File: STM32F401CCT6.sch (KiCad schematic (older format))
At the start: 43 parts, among them J1 USB_OTG, J2 Conn_02x03_Odd_Even, J3 Conn_01x20_des, J4 Conn_01x05_desc, J5 Conn_01x20, SW1 SW_Push, U1 MIC5219-3.3, U2 STM32F401CCT6, U3 USBLC6-2SC6, Y1 32.786K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

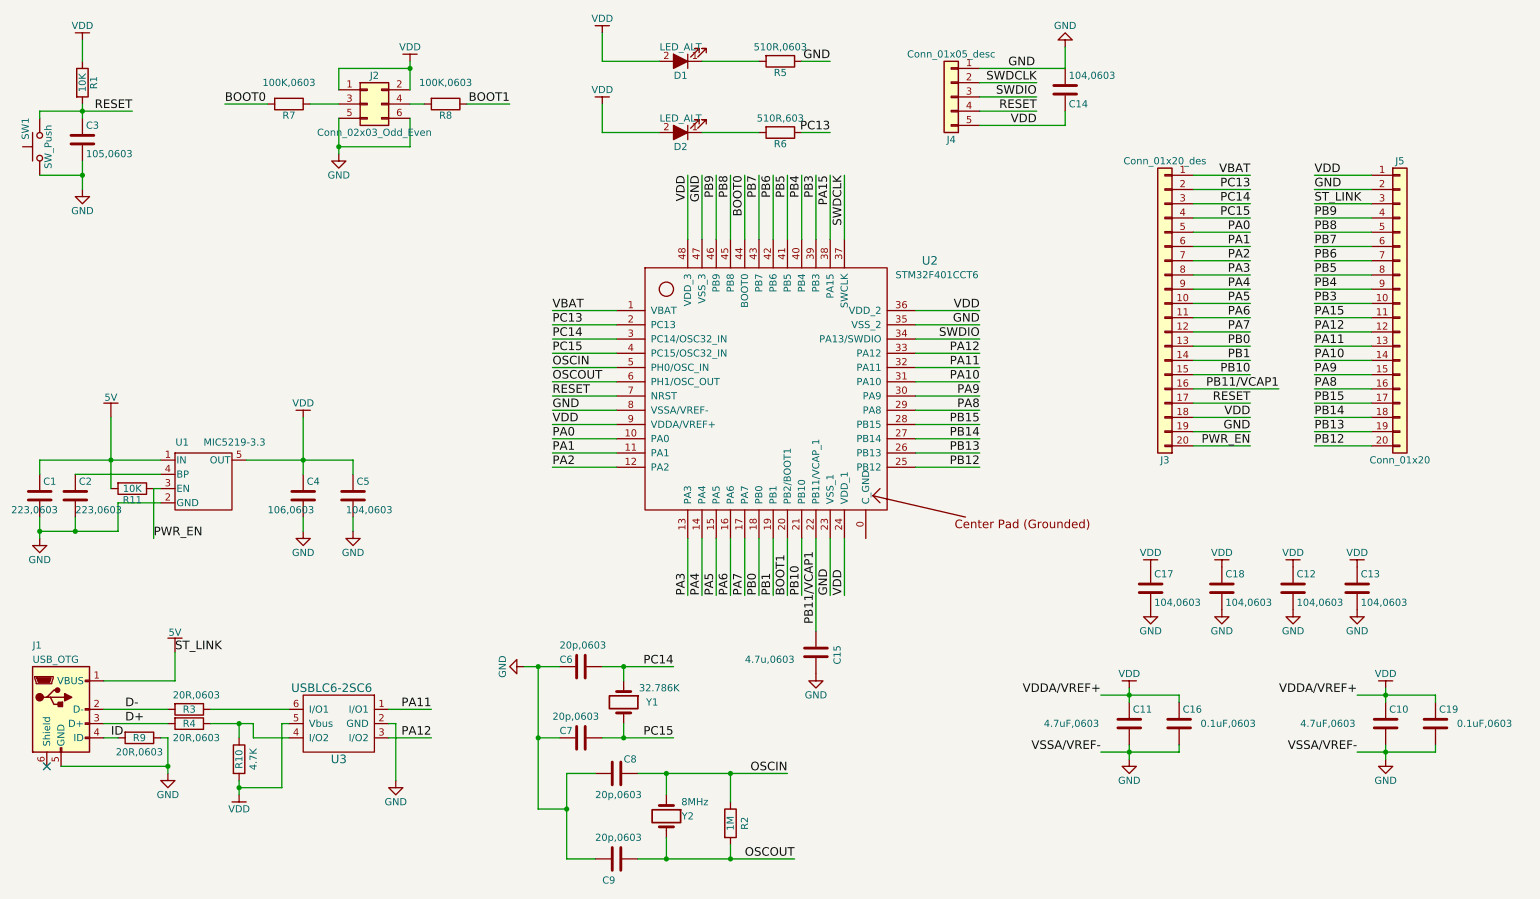
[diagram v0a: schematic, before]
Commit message: Change the route nicely
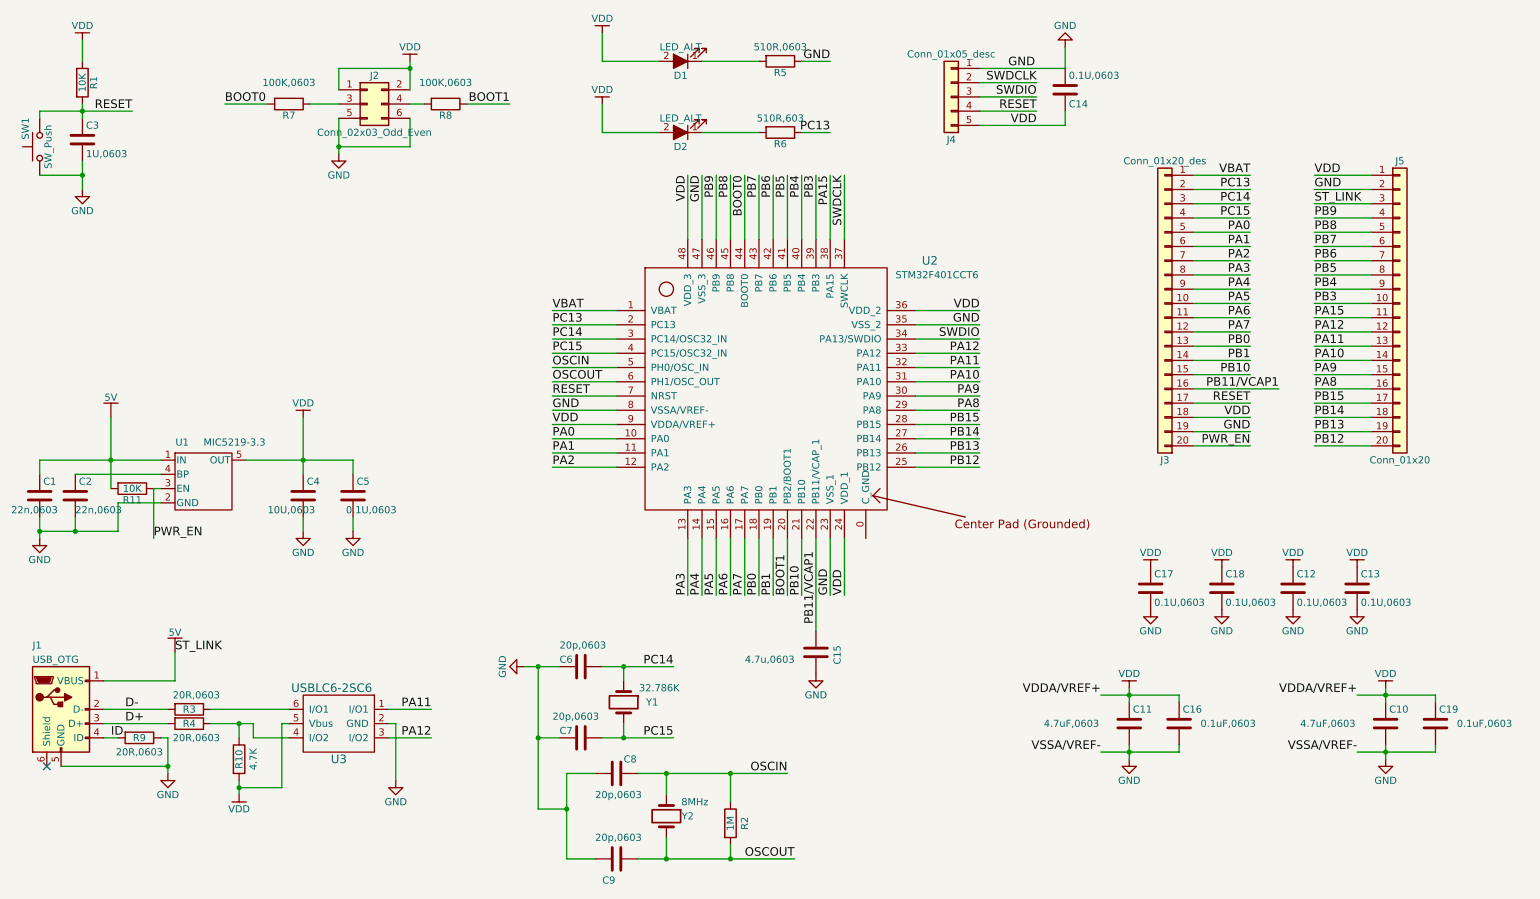
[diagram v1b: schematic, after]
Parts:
- C1, C2: value 223,0603 -> 22n,0603
- C12, C13, C14, C17, C18, C5: value 104,0603 -> 0.1U,0603
- C3: value 105,0603 -> 1U,0603
- C4: value 106,0603 -> 10U,0603
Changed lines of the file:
@@
 P 1050 1600
 F 0 "C3" H 1075 1700 50  0000 L CNN
-F 1 "105,0603" H 1075 1500 50  0000 L CNN
+F 1 "1U,0603" H 1075 1500 50  0000 L CNN
 F 2 "Capacitors_SMD:C_0603" H 1088 1450 50  0001 C CNN
 F 3 "" H 1050 1600 50  0001 C CNN
@@
 P 7950 1250
 F 0 "C14" H 7975 1350 50  0000 L CNN
-F 1 "104,0603" H 7975 1150 50  0000 L CNN
+F 1 "0.1U,0603" H 7975 1150 50  0000 L CNN
 F 2 "Capacitors_SMD:C_0603" H 7988 1100 50  0001 C CNN
 F 3 "" H 7950 1250 50  0001 C CNN
@@
 P 9550 4750
 F 0 "C12" H 9575 4850 50  0000 L CNN
-F 1 "104,0603" H 9575 4650 50  0000 L CNN
+F 1 "0.1U,0603" H 9575 4650 50  0000 L CNN
 F 2 "Capacitors_SMD:C_0603" H 9588 4600 50  0001 C CNN
 F 3 "" H 9550 4750 50  0001 C CNN
@@
 P 10000 4750
 F 0 "C13" H 10025 4850 50  0000 L CNN
-F 1 "104,0603" H 10025 4650 50  0000 L CNN
+F 1 "0.1U,0603" H 10025 4650 50  0000 L CNN
 F 2 "Capacitors_SMD:C_0603" H 10038 4600 50  0001 C CNN
 F 3 "" H 10000 4750 50  0001 C CNN
@@
 P 750 4100
 F 0 "C1" H 775 4200 50  0000 L CNN
-F 1 "223,0603" H 550 4000 50  0000 L CNN
+F 1 "22n,0603" H 550 4000 50  0000 L CNN
 F 2 "Capacitors_SMD:C_0603" H 788 3950 50  0001 C CNN
 F 3 "" H 750 4100 50  0001 C CNN
@@
 P 1000 4100
 F 0 "C2" H 1025 4200 50  0000 L CNN
-F 1 "223,0603" H 1000 4000 50  0000 L CNN
+F 1 "22n,0603" H 1000 4000 50  0000 L CNN
 F 2 "Capacitors_SMD:C_0603" H 1038 3950 50  0001 C CNN
 F 3 "" H 1000 4100 50  0001 C CNN
@@
 P 2600 4100
 F 0 "C4" H 2625 4200 50  0000 L CNN
-F 1 "106,0603" H 2350 4000 50  0000 L CNN
+F 1 "10U,0603" H 2350 4000 50  0000 L CNN
 F 2 "Capacitors_SMD:C_0603" H 2638 3950 50  0001 C CNN
 F 3 "" H 2600 4100 50  0001 C CNN
@@
 P 2950 4100
 F 0 "C5" H 2975 4200 50  0000 L CNN
-F 1 "104,0603" H 2900 4000 50  0000 L CNN
+F 1 "0.1U,0603" H 2900 4000 50  0000 L CNN
 F 2 "Capacitors_SMD:C_0603" H 2988 3950 50  0001 C CNN
 F 3 "" H 2950 4100 50  0001 C CNN
@@
 P 9050 4750
 F 0 "C18" H 9075 4850 50  0000 L CNN
-F 1 "104,0603" H 9075 4650 50  0000 L CNN
+F 1 "0.1U,0603" H 9075 4650 50  0000 L CNN
 F 2 "Capacitors_SMD:C_0603" H 9088 4600 50  0001 C CNN
 F 3 "" H 9050 4750 50  0001 C CNN
@@
 P 8550 4750
 F 0 "C17" H 8575 4850 50  0000 L CNN
-F 1 "104,0603" H 8575 4650 50  0000 L CNN
+F 1 "0.1U,0603" H 8575 4650 50  0000 L CNN
 F 2 "Capacitors_SMD:C_0603" H 8588 4600 50  0001 C CNN
 F 3 "" H 8550 4750 50  0001 C CNN

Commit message: Renamed the pin3 track label from ST-Link to Vin
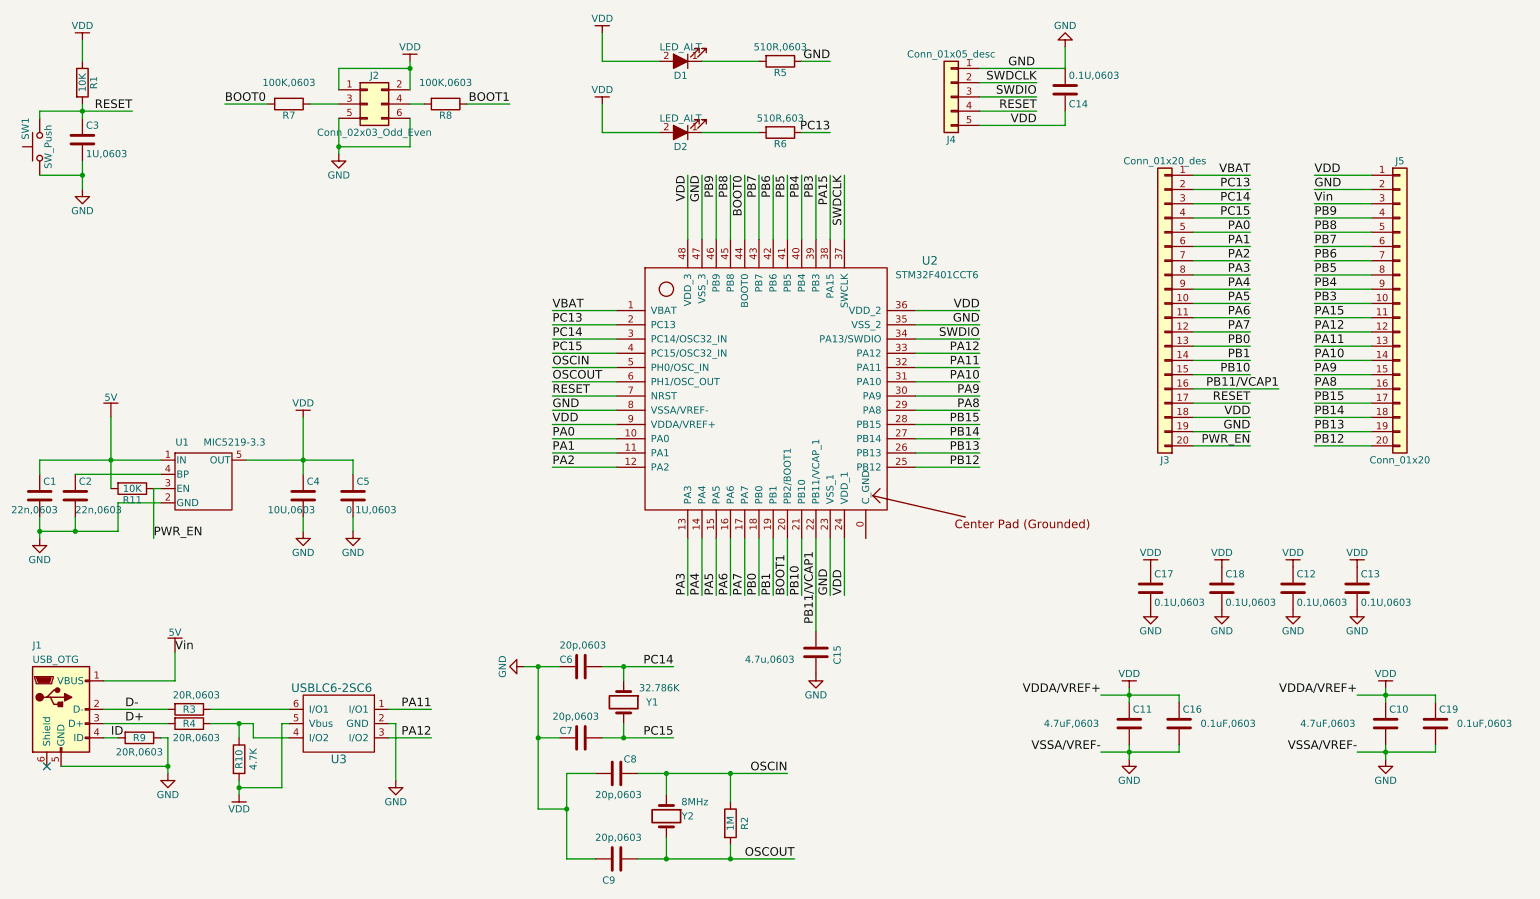
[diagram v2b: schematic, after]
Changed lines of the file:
@@
 GND
 Text Label 9700 2050 0    60   ~ 0
-ST_LINK
+Vin
 Text Label 9700 2150 0    60   ~ 0
 PB9
@@
 GND
 Text Label 1700 5200 0    60   ~ 0
-ST_LINK
+Vin
 $Comp
 L LED_ALT D1

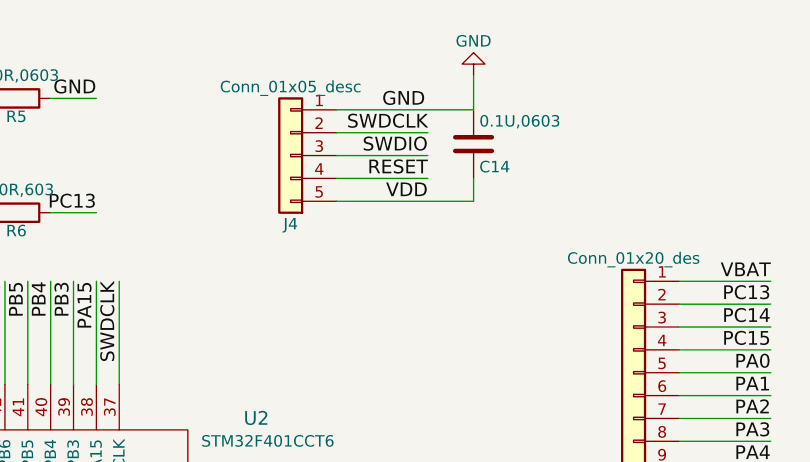
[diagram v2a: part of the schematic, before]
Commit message: Moved silk layer away from via and swap the position of VDD with nRST pin of the SWDIO
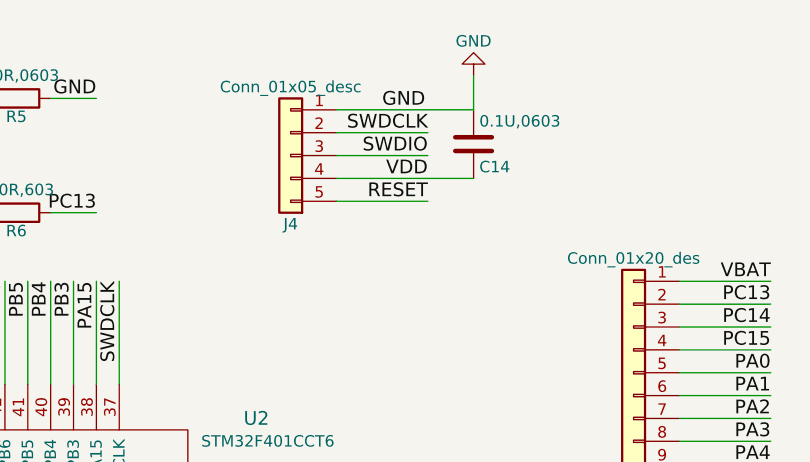
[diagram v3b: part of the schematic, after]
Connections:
- net RESET: now also J4.5 (Pin_5); no longer J4.4 (Pin_4)
- net VDD: now also J4.4 (Pin_4); no longer J4.5 (Pin_5)

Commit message: Replace the Micro-USB footprint with the one newly created, added a shield for MCU (grounded pin), moved some component inwards to prevent touching the pinheader plastic.
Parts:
- D1: value LED_ALT -> RED_LED
- D2: value LED_ALT -> BLUE_LED
- U2: footprint QFPN48:QFN_QFP48 -> (none)
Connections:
- net GND: now also J1.6 (Shield), U2.0 (C_GND)
- no-connect marks 1 -> 0
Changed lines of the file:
@@
 $EndComp
 $Comp
-L GND #PWR01
+L GND #PWR10
 U 1 1 59D25E0A
 P 2850 1700
-F 0 "#PWR01" H 2850 1450 50  0001 C CNN
+F 0 "#PWR10" H 2850 1450 50  0001 C CNN
 F 1 "GND" H 2850 1550 50  0000 C CNN
 F 2 "" H 2850 1700 50  0001 C CNN
@@
 RESET
 $Comp
-L GND #PWR02
+L GND #PWR3
 U 1 1 59D2716C
 P 1050 1950
-F 0 "#PWR02" H 1050 1700 50  0001 C CNN
+F 0 "#PWR3" H 1050 1700 50  0001 C CNN
 F 1 "GND" H 1050 1800 50  0000 C CNN
 F 2 "" H 1050 1950 50  0001 C CNN
@@
 $EndComp
 $Comp
-L 5V #PWR03
+L 5V #PWR6
 U 1 1 59D2797D
 P 1700 5200
-F 0 "#PWR03" H 1700 5050 50  0001 C CNN
+F 0 "#PWR6" H 1700 5050 50  0001 C CNN
 F 1 "5V" H 1700 5340 50  0000 C CNN
 F 2 "" H 1700 5200 50  0001 C CNN
@@
 	1    0    0    -1
 $EndComp
-NoConn ~ 800  6000
 $Comp
 L C C6
@@
 $EndComp
 $Comp
-L GND #PWR04
+L GND #PWR14
 U 1 1 59D289B6
 P 4150 5300
-F 0 "#PWR04" H 4150 5050 50  0001 C CNN
+F 0 "#PWR14" H 4150 5050 50  0001 C CNN
 F 1 "GND" H 4150 5150 50  0000 C CNN
 F 2 "" H 4150 5300 50  0001 C CNN
@@
 $EndComp
 $Comp
-L GND #PWR05
+L GND #PWR31
 U 1 1 59D28EE2
 P 10200 5950
-F 0 "#PWR05" H 10200 5700 50  0001 C CNN
+F 0 "#PWR31" H 10200 5700 50  0001 C CNN
 F 1 "GND" H 10200 5800 50  0000 C CNN
 F 2 "" H 10200 5950 50  0001 C CNN
@@
 $EndComp
 $Comp
-L GND #PWR06
+L GND #PWR27
 U 1 1 59D2CC17
 P 9550 4900
-F 0 "#PWR06" H 9550 4650 50  0001 C CNN
+F 0 "#PWR27" H 9550 4650 50  0001 C CNN
 F 1 "GND" H 9550 4750 50  0000 C CNN
 F 2 "" H 9550 4900 50  0001 C CNN
@@
 $EndComp
 $Comp
-L GND #PWR07
+L GND #PWR29
 U 1 1 59D2CC9A
 P 10000 4900
-F 0 "#PWR07" H 10000 4650 50  0001 C CNN
+F 0 "#PWR29" H 10000 4650 50  0001 C CNN
 F 1 "GND" H 10000 4750 50  0000 C CNN
 F 2 "" H 10000 4900 50  0001 C CNN
@@
 $EndComp
 $Comp
-L GND #PWR08
+L GND #PWR5
 U 1 1 59D2D880
 P 1650 6050
-F 0 "#PWR08" H 1650 5800 50  0001 C CNN
+F 0 "#PWR5" H 1650 5800 50  0001 C CNN
 F 1 "GND" H 1650 5900 50  0000 C CNN
 F 2 "" H 1650 6050 50  0001 C CNN
@@
 $EndComp
 $Comp
-L GND #PWR09
+L GND #PWR1
 U 1 1 59D37486
 P 750 4400
-F 0 "#PWR09" H 750 4150 50  0001 C CNN
+F 0 "#PWR1" H 750 4150 50  0001 C CNN
 F 1 "GND" H 750 4250 50  0000 C CNN
 F 2 "" H 750 4400 50  0001 C CNN
@@
 $EndComp
 $Comp
-L 5V #PWR010
+L 5V #PWR4
 U 1 1 59D374F7
 P 1250 3550
-F 0 "#PWR010" H 1250 3400 50  0001 C CNN
+F 0 "#PWR4" H 1250 3400 50  0001 C CNN
 F 1 "5V" H 1250 3690 50  0000 C CNN
 F 2 "" H 1250 3550 50  0001 C CNN
@@
 $EndComp
 $Comp
-L GND #PWR011
+L GND #PWR9
 U 1 1 59D37C81
 P 2600 4350
-F 0 "#PWR011" H 2600 4100 50  0001 C CNN
+F 0 "#PWR9" H 2600 4100 50  0001 C CNN
 F 1 "GND" H 2600 4200 50  0000 C CNN
 F 2 "" H 2600 4350 50  0001 C CNN
@@
 $EndComp
 $Comp
-L GND #PWR012
+L GND #PWR11
 U 1 1 59D37D1C
 P 2950 4350
-F 0 "#PWR012" H 2950 4100 50  0001 C CNN
+F 0 "#PWR11" H 2950 4100 50  0001 C CNN
 F 1 "GND" H 2950 4200 50  0000 C CNN
 F 2 "" H 2950 4350 50  0001 C CNN
@@
 $EndComp
 $Comp
-L GND #PWR013
+L GND #PWR19
 U 1 1 59D379C4
 P 7950 950
-F 0 "#PWR013" H 7950 700 50  0001 C CNN
+F 0 "#PWR19" H 7950 700 50  0001 C CNN
 F 1 "GND" H 7950 800 50  0000 C CNN
 F 2 "" H 7950 950 50  0001 C CNN
@@
 $EndComp
 $Comp
-L GND #PWR014
+L GND #PWR12
 U 1 1 59D3C918
 P 3250 6100
-F 0 "#PWR014" H 3250 5850 50  0001 C CNN
+F 0 "#PWR12" H 3250 5850 50  0001 C CNN
 F 1 "GND" H 3250 5950 50  0000 C CNN
 F 2 "" H 3250 6100 50  0001 C CNN
@@
 P 5250 1050
 F 0 "D1" H 5250 1150 50  0000 C CNN
-F 1 "LED_ALT" H 5250 950 50  0000 C CNN
+F 1 "RED_LED" H 5250 900 50  0000 C CNN
 F 2 "LEDs:LED_0805" H 5250 1050 50  0001 C CNN
 F 3 "" H 5250 1050 50  0001 C CNN
@@
 P 5250 1550
 F 0 "D2" H 5250 1650 50  0000 C CNN
-F 1 "LED_ALT" H 5250 1450 50  0000 C CNN
+F 1 "BLUE_LED" H 5250 1400 50  0000 C CNN
 F 2 "LEDs:LED_0805" H 5250 1550 50  0001 C CNN
 F 3 "" H 5250 1550 50  0001 C CNN
@@
 PB11/VCAP1
 $Comp
-L GND #PWR015
+L GND #PWR17
 U 1 1 59FD831D
 P 6200 5350
-F 0 "#PWR015" H 6200 5100 50  0001 C CNN
+F 0 "#PWR17" H 6200 5100 50  0001 C CNN
 F 1 "GND" H 6200 5200 50  0000 C CNN
 F 2 "" H 6200 5350 50  0001 C CNN
@@
 $EndComp
 $Comp
-L GND #PWR016
+L GND #PWR21
 U 1 1 5A0064D3
 P 8400 5950
-F 0 "#PWR016" H 8400 5700 50  0001 C CNN
+F 0 "#PWR21" H 8400 5700 50  0001 C CNN
 F 1 "GND" H 8400 5800 50  0000 C CNN
 F 2 "" H 8400 5950 50  0001 C CNN
@@
 $EndComp
 $Comp
-L GND #PWR017
+L GND #PWR25
 U 1 1 5A006C4E
 P 9050 4900
-F 0 "#PWR017" H 9050 4650 50  0001 C CNN
+F 0 "#PWR25" H 9050 4650 50  0001 C CNN
 F 1 "GND" H 9050 4750 50  0000 C CNN
 F 2 "" H 9050 4900 50  0001 C CNN
@@
 $EndComp
 $Comp
-L GND #PWR018
+L GND #PWR23
 U 1 1 5A006D37
 P 8550 4900
-F 0 "#PWR018" H 8550 4650 50  0001 C CNN
+F 0 "#PWR23" H 8550 4650 50  0001 C CNN
 F 1 "GND" H 8550 4750 50  0000 C CNN
 F 2 "" H 8550 4900 50  0001 C CNN
 F 3 "" H 8550 4900 50  0001 C CNN
 	1    8550 4900
-	1    0    0    -1
-$EndComp
-$Comp
-L STM32F401CCT6 U2
-U 1 1 5A00751A
-P 5450 3050
-F 0 "U2" H 7000 3650 60  0000 C CNN
-F 1 "STM32F401CCT6" H 7050 3550 50  0000 C CNN
-F 2 "QFPN48:QFN_QFP48" H 5450 3050 60  0001 C CNN
-F 3 "" H 5450 3050 60  0001 C CNN
-	1    5450 3050
 	1    0    0    -1
 $EndComp
@@
 PWR_EN
 $Comp
-L VDD-RESCUE-STM32F401CCT6 #PWR019
+L VDD-RESCUE-STM32F401CCT6 #PWR13
 U 1 1 5A056104
 P 3350 1050
-F 0 "#PWR019" H 3350 900 50  0001 C CNN
+F 0 "#PWR13" H 3350 900 50  0001 C CNN
 F 1 "VDD" H 3350 1150 50  0000 C CNN
 F 2 "" H 3350 1050 50  0001 C CNN
@@
 $EndComp
 $Comp
-L VDD-RESCUE-STM32F401CCT6 #PWR020
+L VDD-RESCUE-STM32F401CCT6 #PWR2
 U 1 1 5A0564A9
 P 1050 900
-F 0 "#PWR020" H 1050 750 50  0001 C CNN
+F 0 "#PWR2" H 1050 750 50  0001 C CNN
 F 1 "VDD" H 1050 1000 50  0000 C CNN
 F 2 "" H 1050 900 50  0001 C CNN
@@
 $EndComp
 $Comp
-L VDD-RESCUE-STM32F401CCT6 #PWR021
+L VDD-RESCUE-STM32F401CCT6 #PWR15
 U 1 1 5A05668E
 P 4700 850
-F 0 "#PWR021" H 4700 700 50  0001 C CNN
+F 0 "#PWR15" H 4700 700 50  0001 C CNN
 F 1 "VDD" H 4700 950 50  0000 C CNN
 F 2 "" H 4700 850 50  0001 C CNN
@@
 $EndComp
 $Comp
-L VDD-RESCUE-STM32F401CCT6 #PWR022
+L VDD-RESCUE-STM32F401CCT6 #PWR16
 U 1 1 5A056771
 P 4700 1350
-F 0 "#PWR022" H 4700 1200 50  0001 C CNN
+F 0 "#PWR16" H 4700 1200 50  0001 C CNN
 F 1 "VDD" H 4700 1450 50  0000 C CNN
 F 2 "" H 4700 1350 50  0001 C CNN
@@
 $EndComp
 $Comp
-L VDD-RESCUE-STM32F401CCT6 #PWR023
+L VDD-RESCUE-STM32F401CCT6 #PWR22
 U 1 1 5A056DEA
 P 8550 4600
-F 0 "#PWR023" H 8550 4450 50  0001 C CNN
+F 0 "#PWR22" H 8550 4450 50  0001 C CNN
 F 1 "VDD" H 8550 4700 50  0000 C CNN
 F 2 "" H 8550 4600 50  0001 C CNN
@@
 $EndComp
 $Comp
-L VDD-RESCUE-STM32F401CCT6 #PWR024
+L VDD-RESCUE-STM32F401CCT6 #PWR24
 U 1 1 5A0570FB
 P 9050 4600
-F 0 "#PWR024" H 9050 4450 50  0001 C CNN
+F 0 "#PWR24" H 9050 4450 50  0001 C CNN
 F 1 "VDD" H 9050 4700 50  0000 C CNN
 F 2 "" H 9050 4600 50  0001 C CNN
@@
 $EndComp
 $Comp
-L VDD-RESCUE-STM32F401CCT6 #PWR025
+L VDD-RESCUE-STM32F401CCT6 #PWR26
 U 1 1 5A057187
 P 9550 4600
-F 0 "#PWR025" H 9550 4450 50  0001 C CNN
+F 0 "#PWR26" H 9550 4450 50  0001 C CNN
 F 1 "VDD" H 9550 4700 50  0000 C CNN
 F 2 "" H 9550 4600 50  0001 C CNN
@@
 $EndComp
 $Comp
-L VDD-RESCUE-STM32F401CCT6 #PWR026
+L VDD-RESCUE-STM32F401CCT6 #PWR28
 U 1 1 5A057213
 P 10000 4600
-F 0 "#PWR026" H 10000 4450 50  0001 C CNN
+F 0 "#PWR28" H 10000 4450 50  0001 C CNN
 F 1 "VDD" H 10000 4700 50  0000 C CNN
 F 2 "" H 10000 4600 50  0001 C CNN
@@
 $EndComp
 $Comp
-L VDD-RESCUE-STM32F401CCT6 #PWR027
+L VDD-RESCUE-STM32F401CCT6 #PWR20
 U 1 1 5A0574FD
 P 8400 5450
-F 0 "#PWR027" H 8400 5300 50  0001 C CNN
+F 0 "#PWR20" H 8400 5300 50  0001 C CNN
 F 1 "VDD" H 8400 5550 50  0000 C CNN
 F 2 "" H 8400 5450 50  0001 C CNN
@@
 $EndComp
 $Comp
-L VDD-RESCUE-STM32F401CCT6 #PWR028
+L VDD-RESCUE-STM32F401CCT6 #PWR30
 U 1 1 5A057589
 P 10200 5450
-F 0 "#PWR028" H 10200 5300 50  0001 C CNN
+F 0 "#PWR30" H 10200 5300 50  0001 C CNN
 F 1 "VDD" H 10200 5550 50  0000 C CNN
 F 2 "" H 10200 5450 50  0001 C CNN
@@
 $EndComp
 $Comp
-L VDD-RESCUE-STM32F401CCT6 #PWR029
+L VDD-RESCUE-STM32F401CCT6 #PWR8
 U 1 1 5A0578C6
 P 2600 3550
-F 0 "#PWR029" H 2600 3400 50  0001 C CNN
+F 0 "#PWR8" H 2600 3400 50  0001 C CNN
 F 1 "VDD" H 2600 3650 50  0000 C CNN
 F 2 "" H 2600 3550 50  0001 C CNN
@@
 $EndComp
 $Comp
-L VDD-RESCUE-STM32F401CCT6 #PWR030
+L VDD-RESCUE-STM32F401CCT6 #PWR7
 U 1 1 5A057BAF
 P 2150 6200
-F 0 "#PWR030" H 2150 6050 50  0001 C CNN
+F 0 "#PWR7" H 2150 6050 50  0001 C CNN
 F 1 "VDD" H 2150 6300 50  0000 C CNN
 F 2 "" H 2150 6200 50  0001 C CNN
@@
 	-1   0    0    1
 $EndComp
+$Comp
+L STM32F401CCT6 U2
+U 1 1 5A1585BD
+P 5450 3050
+F 0 "U2" H 7000 3650 60  0000 C CNN
+F 1 "STM32F401CCT6" H 7050 3550 50  0000 C CNN
+F 2 "" H 5450 3050 60  0001 C CNN
+F 3 "" H 5450 3050 60  0001 C CNN
+	1    5450 3050
+	1    0    0    -1
+$EndComp
 Wire Wire Line
 	2450 6150 2150 6150
@@
 	2150 6100 2150 6200
 Wire Wire Line
-	900  6000 1650 6000
+	800  6000 1650 6000
 Wire Wire Line
 	1200 5600 1650 5600
@@
 Wire Wire Line
 	7350 1500 7750 1500
+Connection ~ 900  6000
+Wire Wire Line
+	6550 4400 6550 4800
+$Comp
+L GND #PWR18
+U 1 1 5A158D06
+P 6550 4800
+F 0 "#PWR18" H 6550 4550 50  0001 C CNN
+F 1 "GND" H 6550 4650 50  0000 C CNN
+F 2 "" H 6550 4800 50  0001 C CNN
+F 3 "" H 6550 4800 50  0001 C CNN
+	1    6550 4800
+	1    0    0    -1
+$EndComp
 $EndSCHEMATC
